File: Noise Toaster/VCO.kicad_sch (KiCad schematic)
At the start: 37 parts, among them Q1 2N3904, Q2 2N3904, Q3 2N5457, U1 LM324, U2 LM324

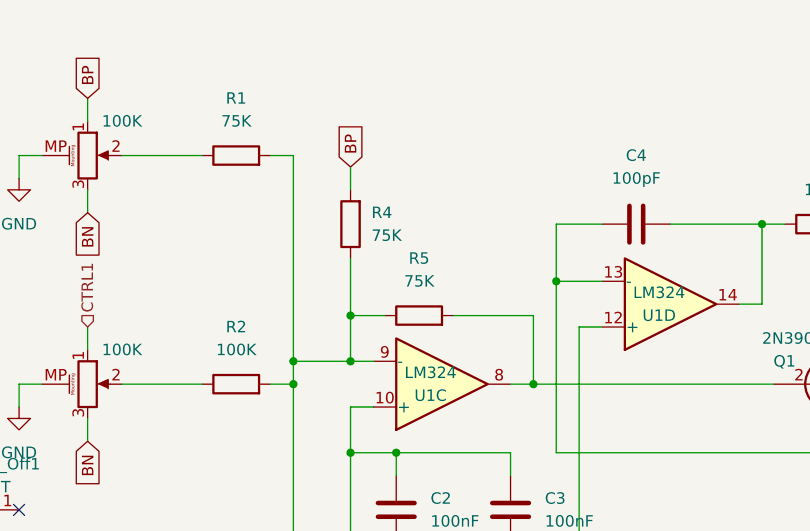
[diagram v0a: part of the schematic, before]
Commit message: Noise Toaster - fixes after first board
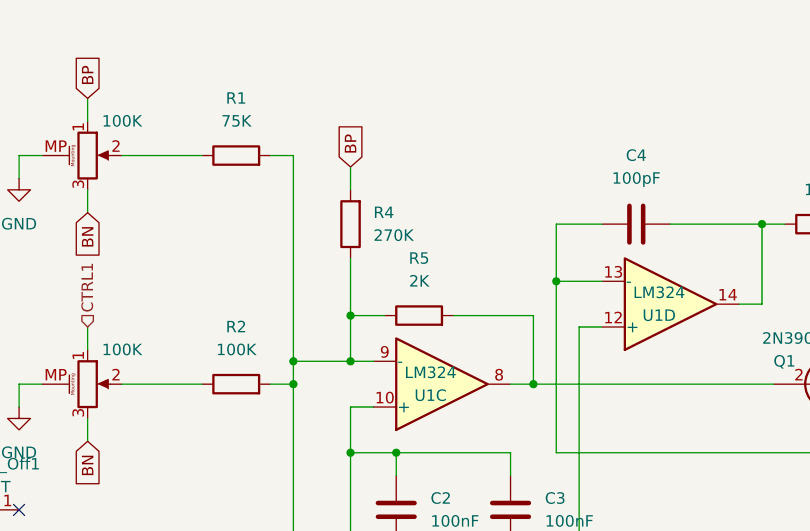
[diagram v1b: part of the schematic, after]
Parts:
- R4: value 75K -> 270K
- R5: value 75K -> 2K
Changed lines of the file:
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@@
   (symbol (lib_id "Device:R") (at 76.2 46.99 180) (unit 1)
     (in_bom yes) (on_board yes) (dnp no) (fields_autoplaced)
-    (property "Reference" "R4" (at 78.5245 45.72 0)
-      (effects (font (size 1.27 1.27)) (justify right))
-    )
-    (property "Value" "75K" (at 78.5245 48.26 0)
+    (property "Reference" "R4" (at 78.74 45.72 0)
+      (effects (font (size 1.27 1.27)) (justify right))
+    )
+    (property "Value" "270K" (at 78.74 48.26 0)
       (effects (font (size 1.27 1.27)) (justify right))
     )
@@
       (effects (font (size 1.27 1.27)))
     )
-    (property "Value" "75K" (at 83.82 53.34 90)
-      (effects (font (size 1.27 1.27)))
-    )
+    (property "Value" "2K" (at 83.82 53.34 90)
+      (effects (font (size 1.27 1.27)))
+    )
